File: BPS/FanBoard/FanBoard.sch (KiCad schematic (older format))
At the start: 19 parts, among them Q1 BUK9M34-100EX, Q2 BUK9M34-100EX, Q3 BUK9M34-100EX, Q4 BUK9M34-100EX

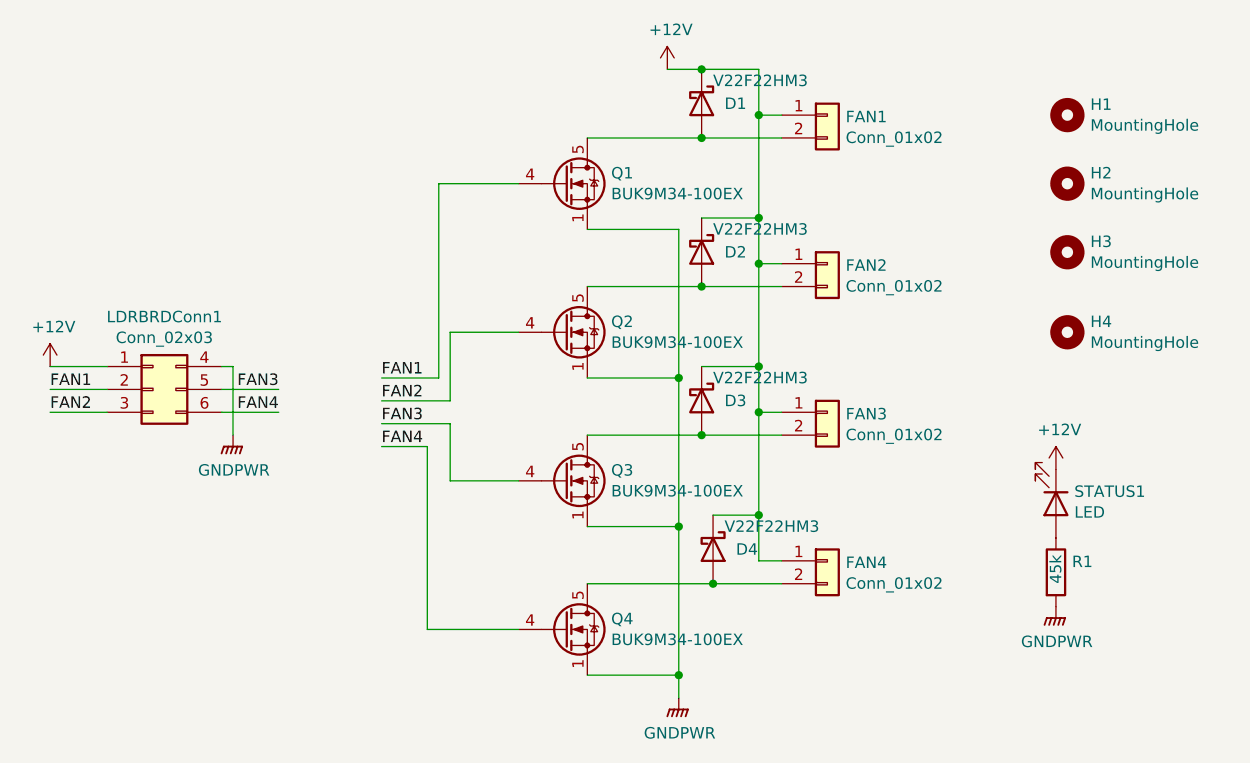
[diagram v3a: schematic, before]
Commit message: Changed location of diodes and direction of status LED. Fixed value and reference labels of components, made pwrgnd plane bigger, and made distance of mounting holes on both sides symmetrical.
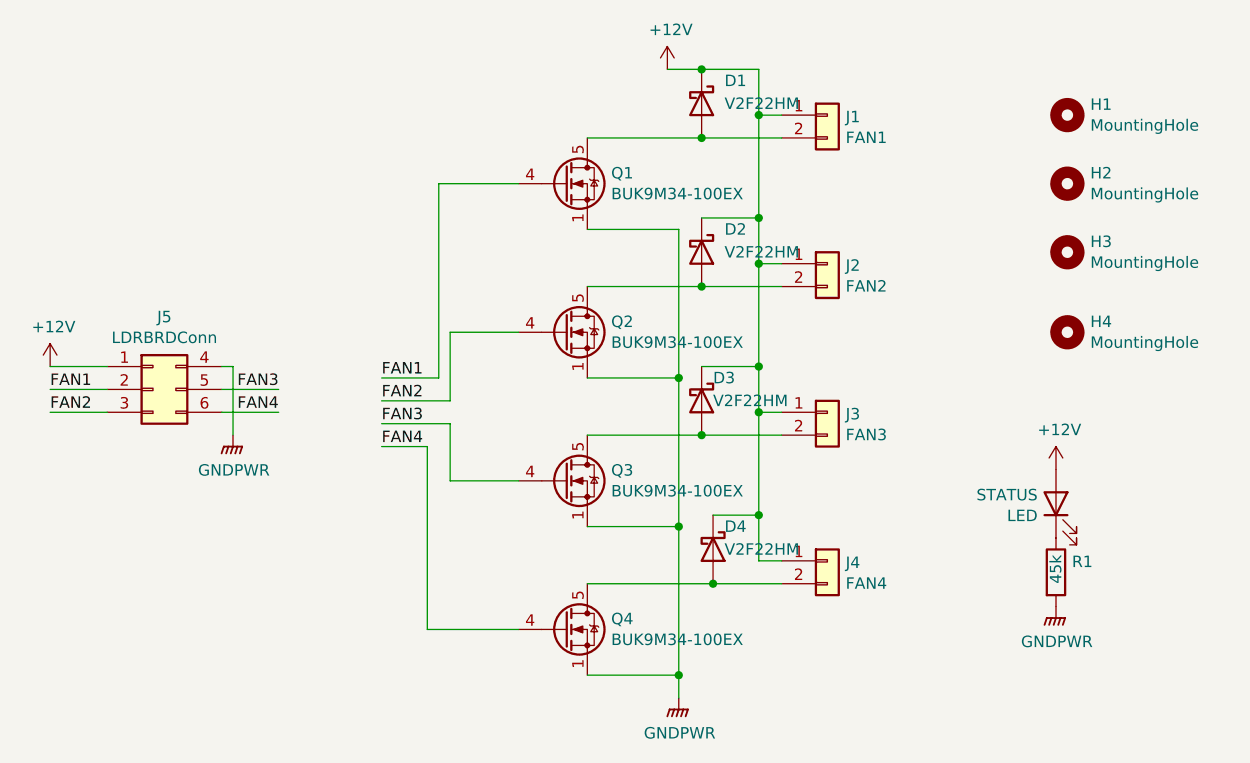
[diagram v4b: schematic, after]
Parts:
- D1, D2, D3, D4: value V22F22HM3 -> V2F22HM
- J1: renamed from FAN1; value Conn_01x02 -> FAN1
- J2: renamed from FAN2; value Conn_01x02 -> FAN2
- J3: renamed from FAN3; value Conn_01x02 -> FAN3
- J4: renamed from FAN4; value Conn_01x02 -> FAN4
- J5: renamed from LDRBRDConn1; value Conn_02x03 -> LDRBRDConn
- LED: renamed from STATUS1; value LED -> STATUS
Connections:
- net +12V: now also LED.2 (A); no longer LED.1 (K)
- net at R1.1: now also LED.1 (K); no longer LED.2 (A)
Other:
- moved on the sheet: LED
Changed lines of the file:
@@
 $EndDescr
 $Comp
-L power:+12V #PWR01
+L power:+12V #PWR03
 U 1 1 5F093D32
 P 3550 3450
-F 0 "#PWR01" H 3550 3300 50  0001 C CNN
+F 0 "#PWR03" H 3550 3300 50  0001 C CNN
 F 1 "+12V" H 3565 3623 50  0000 C CNN
 F 2 "" H 3550 3450 50  0001 C CNN
@@
 	2500 5100 2300 5100
 $Comp
-L power:+12V #PWR03
+L power:+12V #PWR01
 U 1 1 5F1BC556
 P 850 4750
-F 0 "#PWR03" H 850 4600 50  0001 C CNN
+F 0 "#PWR01" H 850 4600 50  0001 C CNN
 F 1 "+12V" H 865 4923 50  0000 C CNN
 F 2 "" H 850 4750 50  0001 C CNN
@@
 $EndComp
 $Comp
-L power:GNDPWR #PWR04
+L power:GNDPWR #PWR02
 U 1 1 5F1BB28B
 P 1650 5050
-F 0 "#PWR04" H 1650 4850 50  0001 C CNN
+F 0 "#PWR02" H 1650 4850 50  0001 C CNN
 F 1 "GNDPWR" H 1654 4896 50  0000 C CNN
 F 2 "" H 1650 5000 50  0001 C CNN
@@
 	1650 4750 1650 5050
 $Comp
-L power:GNDPWR #PWR0101
+L power:GNDPWR #PWR04
 U 1 1 5F1D2CFD
 P 3600 6200
-F 0 "#PWR0101" H 3600 6000 50  0001 C CNN
+F 0 "#PWR04" H 3600 6000 50  0001 C CNN
 F 1 "GNDPWR" H 3604 6046 50  0000 C CNN
 F 2 "" H 3600 6150 50  0001 C CNN
@@
 U 1 1 5F0A3942
 P 3750 5550
-F 0 "D4" V 3750 5650 50  0000 L CNN
-F 1 "V22F22HM3" V 3650 5600 50  0000 L CNN
+F 0 "D4" V 3650 5600 50  0000 L CNN
+F 1 "V2F22HM" V 3750 5600 50  0000 L CNN
 F 2 "UTSVT_BPS:V2F22HM" H 3750 5375 50  0001 C CNN
 F 3 "https://www.wolfspeed.com/media/downloads/103/C3D25170H.pdf" H 3750 5550 50  0001 C CNN
@@
 U 1 1 5F0A37E3
 P 3700 4900
-F 0 "D3" V 3700 5000 50  0000 L CNN
-F 1 "V22F22HM3" V 3600 4950 50  0000 L CNN
+F 0 "D3" V 3600 4950 50  0000 L CNN
+F 1 "V2F22HM" V 3700 4950 50  0000 L CNN
 F 2 "UTSVT_BPS:V2F22HM" H 3700 4725 50  0001 C CNN
 F 3 "https://www.wolfspeed.com/media/downloads/103/C3D25170H.pdf" H 3700 4900 50  0001 C CNN
@@
 U 1 1 5F0A0D46
 P 3700 4250
-F 0 "D2" V 3700 4350 50  0000 L CNN
-F 1 "V22F22HM3" V 3600 4300 50  0000 L CNN
+F 0 "D2" V 3600 4350 50  0000 L CNN
+F 1 "V2F22HM" V 3700 4350 50  0000 L CNN
 F 2 "UTSVT_BPS:V2F22HM" H 3700 4075 50  0001 C CNN
 F 3 "https://www.wolfspeed.com/media/downloads/103/C3D25170H.pdf" H 3700 4250 50  0001 C CNN
@@
 U 1 1 5F0A355E
 P 3700 3600
-F 0 "D1" V 3700 3700 50  0000 L CNN
-F 1 "V22F22HM3" V 3600 3650 50  0000 L CNN
+F 0 "D1" V 3600 3700 50  0000 L CNN
+F 1 "V2F22HM" V 3700 3700 50  0000 L CNN
 F 2 "UTSVT_BPS:V2F22HM" H 3700 3425 50  0001 C CNN
 F 3 "https://www.wolfspeed.com/media/downloads/103/C3D25170H.pdf" H 3700 3600 50  0001 C CNN
@@
 $EndComp
 $Comp
-L Connector_Generic:Conn_02x03_Top_Bottom LDRBRDConn1
+L Connector_Generic:Conn_02x03_Top_Bottom J5
 U 1 1 5F1EEC57
 P 1300 4850
-F 0 "LDRBRDConn1" H 1350 5167 50  0000 C CNN
-F 1 "Conn_02x03" H 1350 5076 50  0000 C CNN
+F 0 "J5" H 1350 5167 50  0000 C CNN
+F 1 "LDRBRDConn" H 1350 5076 50  0000 C CNN
 F 2 "Connector_Molex:Molex_Micro-Fit_3.0_43045-0612_2x03_P3.00mm_Vertical" H 1300 4850 50  0001 C CNN
 F 3 "~" H 1300 4850 50  0001 C CNN
@@
 $EndComp
 $Comp
-L Device:LED STATUS1
+L Device:LED LED
 U 1 1 5F1F72F0
 P 5250 5350
-F 0 "STATUS1" V 5197 5430 50  0000 L CNN
-F 1 "LED" V 5288 5430 50  0000 L CNN
+F 0 "LED" V 5197 5430 50  0000 L CNN
+F 1 "STATUS" V 5288 5430 50  0000 L CNN
 F 2 "LED_SMD:LED_0805_2012Metric" H 5250 5350 50  0001 C CNN
 F 3 "~" H 5250 5350 50  0001 C CNN
 	1    5250 5350
-	0    1    1    0
-$EndComp
-$Comp
-L power:+12V #PWR02
+	0    -1   -1   0
+$EndComp
+$Comp
+L power:+12V #PWR05
 U 1 1 5F1F79F1
 P 5250 5200
-F 0 "#PWR02" H 5250 5050 50  0001 C CNN
+F 0 "#PWR05" H 5250 5050 50  0001 C CNN
 F 1 "+12V" H 5265 5373 50  0000 C CNN
 F 2 "" H 5250 5200 50  0001 C CNN
@@
 $EndComp
 $Comp
-L power:GNDPWR #PWR05
+L power:GNDPWR #PWR06
 U 1 1 5F1F7EC5
 P 5250 5800
-F 0 "#PWR05" H 5250 5600 50  0001 C CNN
+F 0 "#PWR06" H 5250 5600 50  0001 C CNN
 F 1 "GNDPWR" H 5254 5646 50  0000 C CNN
 F 2 "" H 5250 5750 50  0001 C CNN
@@
 $EndComp
 $Comp
-L Connector_Generic:Conn_01x02 FAN4
+L Connector_Generic:Conn_01x02 J4
 U 1 1 5F092946
 P 4250 5600
-F 0 "FAN4" H 4330 5592 50  0000 L CNN
-F 1 "Conn_01x02" H 4330 5501 50  0000 L CNN
+F 0 "J4" H 4330 5592 50  0000 L CNN
+F 1 "FAN4" H 4330 5501 50  0000 L CNN
 F 2 "UTSVT_Connectors:Molex_MicroFit3.0_1x2xP3.00mm_PolarizingPeg_Vertical" H 4250 5600 50  0001 C CNN
 F 3 "~" H 4250 5600 50  0001 C CNN
@@
 $EndComp
 $Comp
-L Connector_Generic:Conn_01x02 FAN3
+L Connector_Generic:Conn_01x02 J3
 U 1 1 5F092588
 P 4250 4950
-F 0 "FAN3" H 4330 4942 50  0000 L CNN
-F 1 "Conn_01x02" H 4330 4851 50  0000 L CNN
+F 0 "J3" H 4330 4942 50  0000 L CNN
+F 1 "FAN3" H 4330 4851 50  0000 L CNN
 F 2 "UTSVT_Connectors:Molex_MicroFit3.0_1x2xP3.00mm_PolarizingPeg_Vertical" H 4250 4950 50  0001 C CNN
 F 3 "~" H 4250 4950 50  0001 C CNN
@@
 $EndComp
 $Comp
-L Connector_Generic:Conn_01x02 FAN2
+L Connector_Generic:Conn_01x02 J2
 U 1 1 5F09203F
 P 4250 4300
-F 0 "FAN2" H 4330 4292 50  0000 L CNN
-F 1 "Conn_01x02" H 4330 4201 50  0000 L CNN
+F 0 "J2" H 4330 4292 50  0000 L CNN
+F 1 "FAN2" H 4330 4201 50  0000 L CNN
 F 2 "UTSVT_Connectors:Molex_MicroFit3.0_1x2xP3.00mm_PolarizingPeg_Vertical" H 4250 4300 50  0001 C CNN
 F 3 "~" H 4250 4300 50  0001 C CNN
@@
 $EndComp
 $Comp
-L Connector_Generic:Conn_01x02 FAN1
+L Connector_Generic:Conn_01x02 J1
 U 1 1 5F091D5D
 P 4250 3650
-F 0 "FAN1" H 4330 3642 50  0000 L CNN
-F 1 "Conn_01x02" H 4330 3551 50  0000 L CNN
+F 0 "J1" H 4330 3642 50  0000 L CNN
+F 1 "FAN1" H 4330 3551 50  0000 L CNN
 F 2 "UTSVT_Connectors:Molex_MicroFit3.0_1x2xP3.00mm_PolarizingPeg_Vertical" H 4250 3650 50  0001 C CNN
 F 3 "~" H 4250 3650 50  0001 C CNN

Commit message: Changes diode footprints to correct path. Need to update netlist and pcb file
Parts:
- D1, D2, D3, D4: footprint UTSVT_BPS:V2F22HM -> UTSVT_Passive:V2F22HM
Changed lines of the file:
@@
 F 0 "D4" V 3650 5600 50  0000 L CNN
 F 1 "V2F22HM" V 3750 5600 50  0000 L CNN
-F 2 "UTSVT_BPS:V2F22HM" H 3750 5375 50  0001 C CNN
+F 2 "UTSVT_Passive:V2F22HM" H 3750 5375 50  0001 C CNN
 F 3 "https://www.wolfspeed.com/media/downloads/103/C3D25170H.pdf" H 3750 5550 50  0001 C CNN
 	1    3750 5550
@@
 F 0 "D3" V 3600 4950 50  0000 L CNN
 F 1 "V2F22HM" V 3700 4950 50  0000 L CNN
-F 2 "UTSVT_BPS:V2F22HM" H 3700 4725 50  0001 C CNN
+F 2 "UTSVT_Passive:V2F22HM" H 3700 4725 50  0001 C CNN
 F 3 "https://www.wolfspeed.com/media/downloads/103/C3D25170H.pdf" H 3700 4900 50  0001 C CNN
 	1    3700 4900
@@
 F 0 "D2" V 3600 4350 50  0000 L CNN
 F 1 "V2F22HM" V 3700 4350 50  0000 L CNN
-F 2 "UTSVT_BPS:V2F22HM" H 3700 4075 50  0001 C CNN
+F 2 "UTSVT_Passive:V2F22HM" H 3700 4075 50  0001 C CNN
 F 3 "https://www.wolfspeed.com/media/downloads/103/C3D25170H.pdf" H 3700 4250 50  0001 C CNN
 	1    3700 4250
@@
 F 0 "D1" V 3600 3700 50  0000 L CNN
 F 1 "V2F22HM" V 3700 3700 50  0000 L CNN
-F 2 "UTSVT_BPS:V2F22HM" H 3700 3425 50  0001 C CNN
+F 2 "UTSVT_Passive:V2F22HM" H 3700 3425 50  0001 C CNN
 F 3 "https://www.wolfspeed.com/media/downloads/103/C3D25170H.pdf" H 3700 3600 50  0001 C CNN
 	1    3700 3600
